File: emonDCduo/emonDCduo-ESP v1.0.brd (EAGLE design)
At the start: 99.1 x 76.5 mm, 86 parts, among them Q1 16Mhz XT49M-2016M, U1_TQFP ATMEGA328P

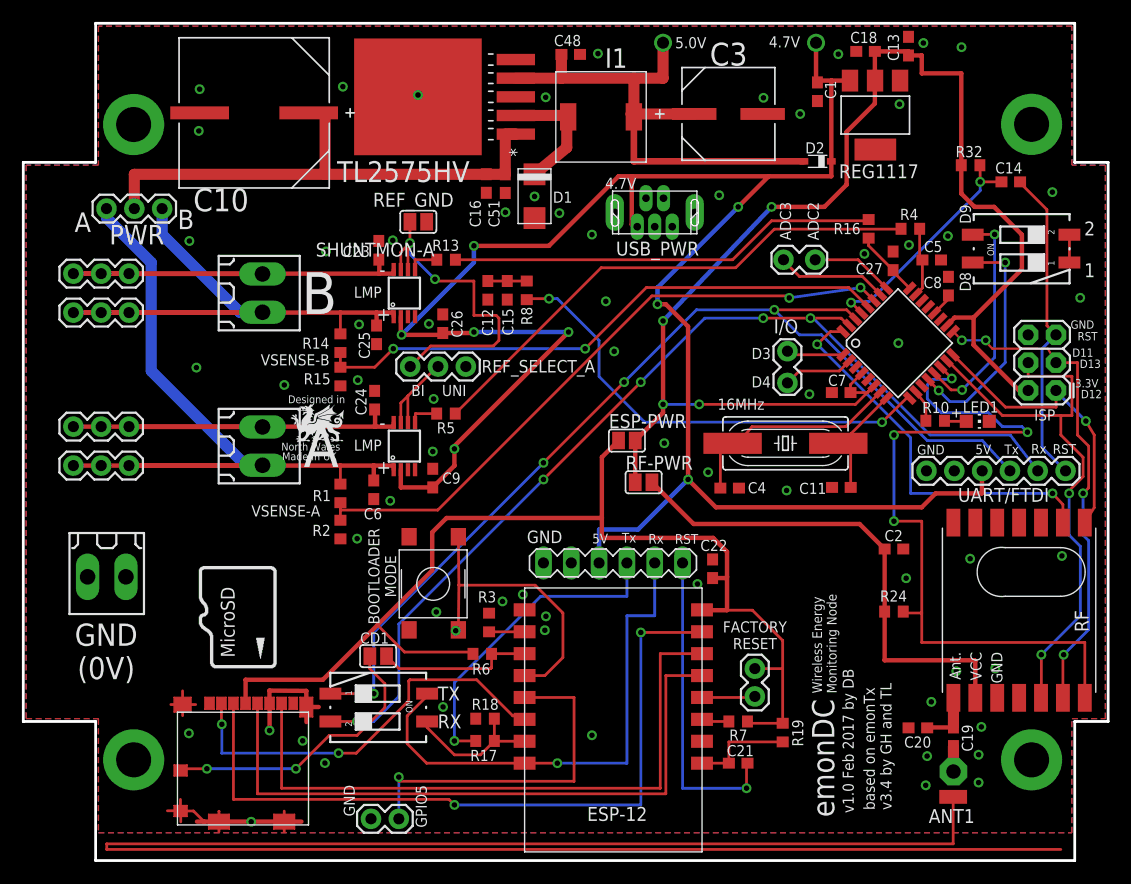
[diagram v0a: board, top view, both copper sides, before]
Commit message: update
chip select set to GPIO4 for both mini and duo.
mini updated, various minor changes for v0.5.
molex micro sd card library improved
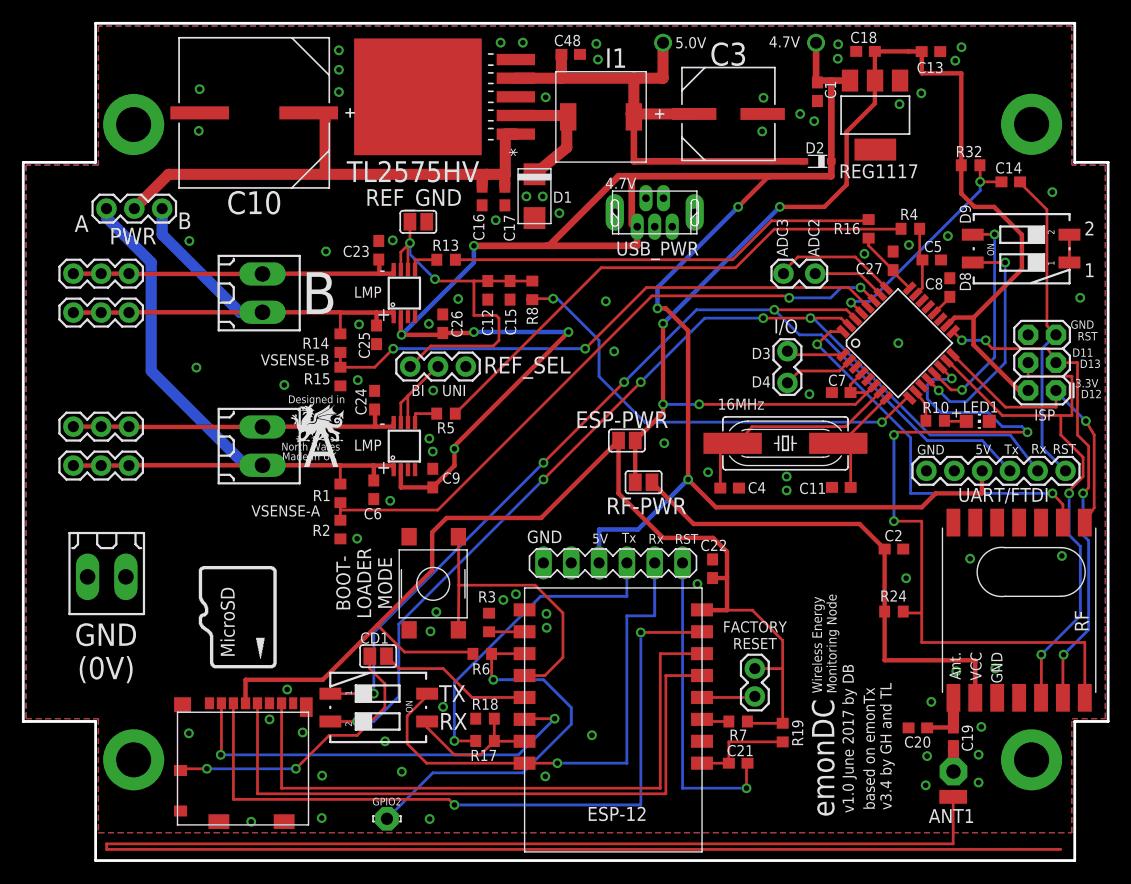
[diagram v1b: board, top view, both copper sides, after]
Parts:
- removed C51: 0.1uF 100V, rcl:C0603
- removed IO2: (no value), SparkFun:1X02
- added C17: 0.1uF 100V, rcl:C0603
- added GPIO2: LSP11, solpad:LSP11
- moved ANA 2.84 mm to (69.8, 55.4), turned to 0 degrees
- moved LOGO1 2.42 mm to (22.9, 18.2)
- moved C13 2.11 mm to (83.1, 75.6), turned to 0 degrees
- moved C16 1.20 mm to (42.2, 62.5)
- moved R8 0.51 mm to (46.7, 53.8)
- moved C15 0.25 mm to (44.7, 53.8)
- moved C8 0.18 mm to (84.9, 54.1)
- renumbered REF_SELECT_A to REF_SEL
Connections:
- net GND: now also C17.2; no longer C51.2, IO2.1
- net GPIO2: now also GPIO2.MP; no longer CD1.2
- net GPIO5: now also CD1.2; no longer IO2.2
- net PWR_IN: now also C17.1; no longer C51.1
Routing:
- net N$5: track 0.00 -> 168.7 mm
- net N$31: track 168.7 -> 0.00 mm
- net GND: track 37.8 -> 3.43 mm, vias 70 -> 86
- net GPIO2: track 14.4 -> 35.5 mm, vias 0 -> 1
- net GPIO5: track 32.4 -> 14.2 mm, vias 1 -> 0
- net LOAD-NEG-B: track 48.9 -> 31.0 mm
- net SOURCE-POS-B: track 64.8 -> 47.2 mm
- net LOAD-NEG-A: track 48.6 -> 31.3 mm
- net SOURCE-POS-A: track 76.1 -> 64.2 mm
- net 4.7V: track 185.0 -> 194.2 mm
- net ADC2: track 7.59 -> 11.3 mm
- net ADC3: track 10.2 -> 6.74 mm
- net GPIO4: track 37.6 -> 39.8 mm
- net REFINPUT: track 35.3 -> 37.1 mm
- net D5/PWM0: track 42.7 -> 43.4 mm
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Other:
- board text added: "BOOT- LOADER MODE"
- board text added: "v1.0 June 2017 by DB"
- board text removed: "BOOTLOADER MODE"
- board text removed: "GPIO5"
- board text removed: "v1.0 Feb 2017 by DB"

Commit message: commit
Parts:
- moved R32 1.40 mm to (86.8, 66.7)
- moved C10 1.21 mm to (22.5, 69.7), turned to 90 degrees
- moved C13 0.40 mm to (83.3, 75.3)
- moved C18 0.38 mm to (77.2, 75.3)
- moved D1 0.38 mm to (47.3, 62.4)
- moved C7 0.33 mm to (74.6, 44.5)
- moved RF 0.30 mm to (91.2, 24.9)
- moved C16 0.13 mm to (42.2, 62.3)
- moved C17 0.13 mm to (44.2, 62.3)
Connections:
- net 3.3V: now also REG1117.4
- net GPIO15: now also U$2.P$2
- net GPIO4: now also CD1.2; no longer U$2.P$2
- net GPIO5: no longer CD1.2
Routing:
- net GPIO15: track 3.25 -> 52.0 mm, vias 0 -> 2
- net GPIO4: track 39.8 -> 15.0 mm, vias 2 -> 0
- net GPIO5: track 14.2 -> 0.00 mm
- net 3.3V: track 125.5 -> 117.6 mm
- net PWR_IN: track 50.1 -> 43.7 mm
- net N$13: track 0.00 -> 6.35 mm
- net N$2: track 0.00 -> 6.33 mm
- net RESET2: track 21.7 -> 24.4 mm
- net DIG1: track 5.14 -> 5.72 mm
- net GND: vias 86 -> 87

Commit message: v1.0 duo camexport and prototype
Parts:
- removed C12, C15: 100nF, rcl:C0603
- removed R8: 3.9K, rcl:R0603
- removed REF_GND: (no value), jumper:SJ
- removed REF_SEL: 2212S-02SG-85, SparkFun-Connectors:1X03
- added R11: 30K, rcl:R0603
- added R9: 10K, rcl:R0603
- added REF_SEL_A, REF_SEL_B: 2212S-02SG-85, SparkFun-Connectors:1X03
- moved C26 0.90 mm to (39.4, 50.6)
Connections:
- removed net N$11: REF_SEL.2, SHUNTMON-B.6, SHUNTMON-B.7
- removed net REFINPUT: C12.1, C15.1, R8.1, REF_GND.1, REF_SEL.1, SHUNTMON-A.6, SHUNTMON-A.7
- new net REF_A_INPUT: REF_SEL_A.2, SHUNTMON-B.6, SHUNTMON-B.7
- new net REF_B_INPUT: REF_SEL_B.2, SHUNTMON-A.6, SHUNTMON-A.7
- new net REF_INPUT: R11.2, R9.1, REF_SEL_A.1, REF_SEL_B.3
- net 4.7V: now also R9.2
- net D5/PWM0: no longer R8.2
- net GND: now also R11.1, REF_SEL_A.3, REF_SEL_B.1; no longer C12.2, C15.2, REF_GND.2, REF_SEL.3
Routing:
- net D5/PWM0: track 43.5 -> 0.00 mm, vias 2 -> 0
- net REFINPUT: track 37.1 -> 0.00 mm, vias 2 -> 0
- net REF_INPUT: track 0.00 -> 22.5 mm, vias 0 -> 1
- net N$11: track 8.98 -> 0.00 mm
- net REF_B_INPUT: track 0.00 -> 8.73 mm
- net REF_A_INPUT: track 0.00 -> 8.72 mm
- net 4.7V: track 194.2 -> 199.1 mm, vias 9 -> 10
- net GND: vias 87 -> 91
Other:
- board text added: "v1.0 July 2017 by DB"
- board text removed: "v1.0 June 2017 by DB"
